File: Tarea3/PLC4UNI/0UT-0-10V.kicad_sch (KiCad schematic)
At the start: 0 parts

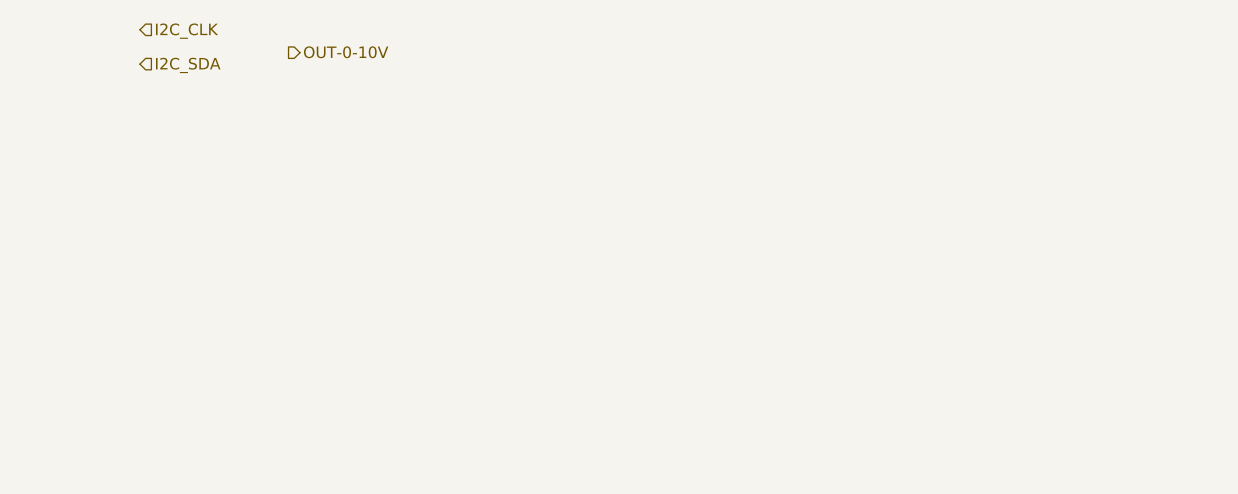
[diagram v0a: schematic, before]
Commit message: Cambio de directorio [Tarea2->CAD]
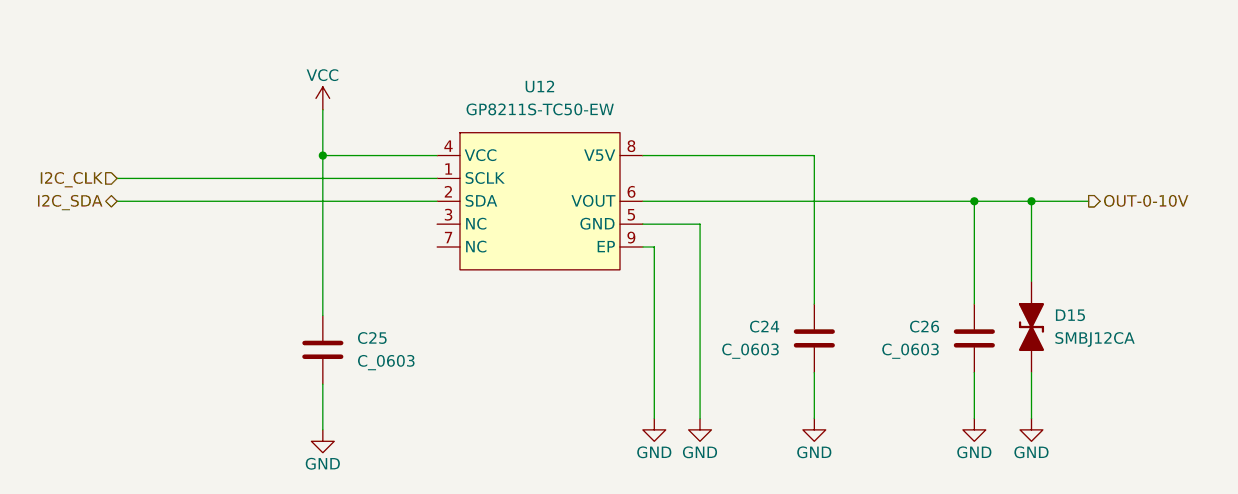
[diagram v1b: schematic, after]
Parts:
- added C24, C25, C26: C_0603, PCM_Capacitor_SMD_AKL:C_0603_1608Metric, symbol PCM_Capacitor_US_AKL:C_0603
- added D15: SMBJ12CA, PCM_Diode_SMD_AKL:D_SMB_TVS, symbol PCM_Diode_TVS_AKL:SMBJ12CA
- added U12: GP8211S-TC50-EW, EasyEDA:ESOP-8_L4.9-W3.9-P1.27-LS6.0-BL-EP, symbol EasyEDA:GP8211S-TC50-EW
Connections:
- net I2C_CLK: now also U12.1 (SCLK)
- net I2C_SDA: now also U12.2 (SDA)
- net OUT-0-10V: now also C26.1, D15.2 (A), U12.6 (VOUT)
- new net: C24.1, U12.8 (V5V)
- new net GND: C24.2, C25.2, C26.2, D15.1 (K), U12.5 (GND), U12.9 (EP)
- new net VCC: C25.1, U12.4 (VCC)
